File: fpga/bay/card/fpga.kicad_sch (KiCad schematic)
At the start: 0 parts

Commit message: card: fpga sheet — U14 XCAU15P placed and every ball resolved (rails, config, Quad 225, bank 84, unused banks/quads per 0011); passives next
Co-Authored-By: Claude Opus 5.5 (1M context) <noreply@anthropic.com>
Claude-Session: https://claude.ai/code/session_019QA2U79cSHCaAaMe6Km575
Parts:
- added U14: XCAU15P-2FFVB676E, symbol fw16-fpga-module:XCAU15P-FFVB676
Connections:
- new net +0V85_VCCINT: U14.K11 (VCCINT), U14.K13 (VCCINT), U14.K15 (VCCINT), U14.K17 (VCCINT), U14.L10 (VCCINT), U14.L12 (VCCINT), U14.L14 (VCCINT), U14.L16 (VCCINT), U14.L9 (VCCINT_IO), U14.M11 (VCCINT), U14.M13 (VCCINT), U14.M15 (VCCINT), U14.M17 (VCCINT), U14.M9 (VCCINT_IO), U14.N10 (VCCINT), U14.N12 (VCCINT), U14.N16 (VCCINT), U14.N9 (VCCINT_IO), U14.P11 (VCCINT), U14.P15 (VCCINT), U14.P17 (VCCINT), U14.P9 (VCCINT_IO), U14.R10 (VCCINT), U14.R12 (VCCINT), U14.R16 (VCCINT), U14.R9 (VCCBRAM), U14.T11 (VCCINT), U14.T15 (VCCINT), U14.T17 (VCCINT), U14.T9 (VCCBRAM), U14.U10 (VCCINT), U14.U12 (VCCINT), U14.U14 (VCCINT), U14.U16 (VCCINT), U14.U9 (VCCBRAM), U14.V11 (VCCINT), U14.V13 (VCCINT), U14.V15 (VCCINT), U14.V17 (VCCINT), U14.V9 (VCCBRAM)
- new net +0V9_MGTAVCC: U14.AA7 (MGTAVCC_R), U14.AC7 (MGTAVCC_R), U14.J7 (MGTAVCC_R), U14.L7 (MGTAVCC_R), U14.N7 (MGTAVCC_R), U14.W7 (MGTAVCC_R)
- new net +1V2_MGTAVTT: U14.A7 (MGTAVTT_R), U14.AB5 (MGTAVTT_R), U14.AD8 (MGTAVTTRCAL_R), U14.AE7 (MGTAVTT_R), U14.C7 (MGTAVTT_R), U14.E7 (MGTAVTT_R), U14.F5 (MGTAVTT_R), U14.G7 (MGTAVTT_R), U14.H5 (MGTAVTT_R), U14.K5 (MGTAVTT_R), U14.M5 (MGTAVTT_R), U14.P5 (MGTAVTT_R), U14.T5 (MGTAVTT_R), U14.V5 (MGTAVTT_R), U14.Y5 (MGTAVTT_R)
- new net +1V8: U14.AA11 (VCCO_0), U14.AA21 (VCCO_64), U14.AB18 (VCCO_64), U14.AD12 (VCCO_0), U14.AD22 (VCCO_64), U14.E14 (VCCO_86), U14.E24 (VCCO_66), U14.E9 (VCCO_85), U14.H10 (VCCO_85), U14.H15 (VCCO_86), U14.H25 (VCCO_66), U14.J22 (VCCO_66), U14.M18 (VCCAUX), U14.N18 (VCCAUX), U14.P18 (VCCAUX_IO), U14.P22 (VCCO_65), U14.R18 (VCCAUX_IO), U14.T18 (VCCAUX_IO), U14.U23 (VCCO_65), U14.Y24 (VCCO_65)
- new net +1V8_MGTVCCAUX: U14.R7 (MGTVCCAUX_R), U14.U7 (MGTVCCAUX_R)
- new net +3V3_IO: U14.AC15 (VCCO_84), U14.Y14 (VCCO_84)
- new net CLK100M: U14.AC13 (IO_L5P_HDGC_AD7P_84)
- new net FPGA_CCLK: U14.Y11 (CCLK_0)
- new net FPGA_CLKREQ_N: U14.AF15 (IO_L1N_AD11N_84)
- new net FPGA_D00: U14.AD11 (D00_MOSI_0)
- new net FPGA_D01: U14.AC12 (D01_DIN_0)
- new net FPGA_D02: U14.AC11 (D02_0)
- new net FPGA_D03: U14.AE11 (D03_0)
- new net FPGA_DONE: U14.AB11 (DONE_0)
- new net FPGA_FCS_B: U14.AA12 (RDWR_FCS_B_0)
- new net FPGA_INIT_B: U14.W10 (INIT_B_0)
- new net FPGA_M0: U14.AA10 (M0_0)
- new net FPGA_M1: U14.AA9 (M1_0)
- new net FPGA_M2: U14.AF12 (M2_0)
- new net FPGA_PROGRAM_B: U14.AB9 (PROGRAM_B_0)
- new net FPGA_PUDC_B: U14.W9 (PUDC_B_0)
- new net FPGA_TCK: U14.AE12 (TCK_0)
- new net FPGA_TDI: U14.AB12 (TDI_0)
- new net FPGA_TDO: U14.Y10 (TDO_0)
- new net FPGA_TH_ALERT: U14.AE13 (IO_L2P_AD10P_84)
- new net FPGA_TH_OVERT: U14.AF13 (IO_L2N_AD10N_84)
- new net FPGA_TMS: U14.AB10 (TMS_0)
- new net GND: U14.A1 (GND), U14.A11 (GND), U14.A16 (GND), U14.A2 (GND), U14.A21 (GND), U14.A26 (GND), U14.A5 (GND), U14.A6 (GND), U14.A8 (GND), U14.AA1 (GND), U14.AA16 (GND), U14.AA2 (GND), U14.AA26 (GND), U14.AA3 (GND), U14.AA6 (GND), U14.AA8 (GND), U14.AB1 (MGTHRXN3_224), U14.AB13 (GND), U14.AB2 (MGTHRXP3_224), U14.AB23 (GND), U14.AB3 (GND), U14.AB4 (GND), U14.AB8 (GND), U14.AC1 (GND), U14.AC10 (GND), U14.AC2 (GND), U14.AC20 (GND), U14.AC25 (GND), U14.AC3 (GND), U14.AC6 (GND), U14.AC8 (GND), U14.AC9 (GND), U14.AD1 (MGTHRXN2_224), U14.AD10 (GND), U14.AD17 (GND), U14.AD2 (MGTHRXP2_224), U14.AD3 (GND), U14.AD4 (GND), U14.AD5 (GND), U14.AE1 (GND), U14.AE10 (GND), U14.AE14 (GND), U14.AE19 (GND), U14.AE2 (GND), U14.AE24 (GND), U14.AE3 (MGTHRXN1_224), U14.AE4 (MGTHRXP1_224), U14.AE5 (GND), U14.AE6 (GND), U14.AF1 (MGTHRXN0_224), U14.AF10 (GND), U14.AF11 (GND), U14.AF16 (GND), U14.AF2 (MGTHRXP0_224), U14.AF21 (GND), U14.AF26 (GND), U14.AF3 (GND), U14.AF4 (GND), U14.AF5 (GND), U14.AF8 (GND), U14.AF9 (GND), U14.B13 (GND), U14.B18 (GND), U14.B23 (GND), U14.B3 (GND), U14.B4 (GND), U14.B5 (GND), U14.B8 (GND), U14.C1 (GND), U14.C10 (GND), U14.C15 (GND), U14.C2 (GND), U14.C25 (GND), U14.C5 (GND), U14.C6 (GND), U14.C8 (GND), U14.D12 (GND), U14.D22 (GND), U14.D3 (GND), U14.D4 (GND), U14.D5 (GND), U14.D8 (GND), U14.E1 (GND), U14.E19 (GND), U14.E2 (GND), U14.E3 (GND), U14.E6 (GND), U14.E8 (GND), U14.F1 (MGTHRXN3_226), U14.F11 (GND), U14.F16 (GND), U14.F2 (MGTHRXP3_226), U14.F21 (GND), U14.F26 (GND), U14.F3 (GND), U14.F4 (GND), U14.F8 (GND), U14.G1 (GND), U14.G13 (GND), U14.G2 (GND), U14.G23 (GND), U14.G3 (GND), U14.G6 (GND), U14.G8 (GND), U14.H1 (MGTHRXN2_226), U14.H2 (MGTHRXP2_226), U14.H20 (GND), U14.H3 (GND), U14.H4 (GND), U14.H8 (GND), U14.J1 (GND), U14.J17 (GND), U14.J2 (GND), U14.J3 (GND), U14.J6 (GND), U14.J8 (GND), U14.K1 (MGTHRXN1_226), U14.K12 (GND), U14.K14 (GND), U14.K16 (GND), U14.K19 (GND), U14.K2 (MGTHRXP1_226), U14.K24 (GND), U14.K3 (GND), U14.K4 (GND), U14.K8 (GND), U14.L1 (GND), U14.L11 (GND), U14.L13 (GND), U14.L15 (GND), U14.L17 (GND), U14.L2 (GND), U14.L21 (GND), U14.L26 (GND), U14.L3 (GND), U14.L6 (GND), U14.L8 (GND), U14.M1 (MGTHRXN0_226), U14.M10 (GND), U14.M12 (GND), U14.M14 (GND), U14.M16 (GND), U14.M2 (MGTHRXP0_226), U14.M23 (GND), U14.M3 (GND), U14.M4 (GND), U14.M8 (GND), U14.N1 (GND), U14.N11 (GND), U14.N15 (GND), U14.N17 (GND), U14.N2 (GND), U14.N20 (GND), U14.N25 (GND), U14.N3 (GND), U14.N6 (GND), U14.N8 (GND), U14.P10 (GND), U14.P12 (GND), U14.P16 (GND), U14.P3 (GND), U14.P4 (GND), U14.P8 (GND), U14.R1 (GND), U14.R11 (GND), U14.R15 (GND), U14.R17 (GND), U14.R19 (GND), U14.R2 (GND), U14.R24 (GND), U14.R3 (GND), U14.R6 (GND), U14.R8 (GND), U14.T10 (GND), U14.T12 (GND), U14.T13 (DXN), U14.T14 (DXP), U14.T16 (GND), U14.T21 (GND), U14.T26 (GND), U14.T3 (GND), U14.T4 (GND), U14.T8 (GND), U14.U1 (GND), U14.U11 (GND), U14.U13 (GND), U14.U15 (GND), U14.U17 (GND), U14.U18 (GND), U14.U2 (GND), U14.U3 (GND), U14.U6 (GND), U14.U8 (GND), U14.V10 (GND), U14.V12 (GND), U14.V14 (GND), U14.V16 (GND), U14.V20 (GND), U14.V25 (GND), U14.V3 (GND), U14.V4 (GND), U14.V8 (GND), U14.W1 (GND), U14.W11 (RSVDGND), U14.W17 (GND), U14.W2 (GND), U14.W22 (GND), U14.W3 (GND), U14.W6 (GND), U14.W8 (GND), U14.Y12 (POR_OVERRIDE), U14.Y19 (GND), U14.Y3 (GND), U14.Y4 (GND), U14.Y8 (GND), U14.Y9 (VBATT)
- new net GNDADC: U14.N13 (GNDADC), U14.P13 (VREFN), U14.P14 (VP), U14.R13 (VN), U14.R14 (VREFP)
- new net GT_REFCLK0_N: U14.V6 (MGTREFCLK0N_225)
- new net GT_REFCLK0_P: U14.V7 (MGTREFCLK0P_225)
- new net GT_REFCLK1_N: U14.T6 (MGTREFCLK1N_225)
- new net GT_REFCLK1_P: U14.T7 (MGTREFCLK1P_225)
- new net GT_TX0_N: U14.AA4 (MGTHTXN0_225)
- new net GT_TX0_P: U14.AA5 (MGTHTXP0_225)
- new net GT_TX1_N: U14.W4 (MGTHTXN1_225)
- new net GT_TX1_P: U14.W5 (MGTHTXP1_225)
- new net GT_TX2_N: U14.U4 (MGTHTXN2_225)
- new net GT_TX2_P: U14.U5 (MGTHTXP2_225)
- new net GT_TX3_N: U14.R4 (MGTHTXN3_225)
- new net GT_TX3_P: U14.R5 (MGTHTXP3_225)
- new net LED_HB: U14.W12 (IO_L12P_AD0P_84)
- new net LED_LINK: U14.W13 (IO_L12N_AD0N_84)
- new net MGT_RREF: U14.AD9 (MGTRREF_R)
- new net PEX_RST#: U14.AF14 (IO_L1P_AD11P_84)
- new net PEX_TX0_N: U14.Y1 (MGTHRXN0_225)
- new net PEX_TX0_P: U14.Y2 (MGTHRXP0_225)
- new net PEX_TX1_N: U14.V1 (MGTHRXN1_225)
- new net PEX_TX1_P: U14.V2 (MGTHRXP1_225)
- new net PEX_TX2_N: U14.T1 (MGTHRXN2_225)
- new net PEX_TX2_P: U14.T2 (MGTHRXP2_225)
- new net PEX_TX3_N: U14.P1 (MGTHRXN3_225)
- new net PEX_TX3_P: U14.P2 (MGTHRXP3_225)
- new net PPS_IN: U14.AB15 (IO_L6P_HDGC_AD6P_84)
- new net SENSE_ALERT#: U14.AD14 (IO_L4N_AD8N_84)
- new net SENSE_SCL: U14.AD15 (IO_L3P_AD9P_84)
- new net SENSE_SDA: U14.AE15 (IO_L3N_AD9N_84)
- new net VCCADC: U14.N14 (VCCADC)
- no-connect marks 0 -> 244

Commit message: card: fpga sheet complete — decoupling, SYSMON filter, RCAL, PCIe AC caps, SiT8008/SiT9121 clocks, U.FL PPS/ref input, LEDs; card ERC 0 errors
Co-Authored-By: Claude Opus 5.5 (1M context) <noreply@anthropic.com>
Claude-Session: https://claude.ai/code/session_019QA2U79cSHCaAaMe6Km575
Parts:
- added C46: 330u/2.5V polymer, Capacitor_Tantalum_SMD:CP_EIA-7343-31_Kemet-D, symbol Device:C_Polarized
- added C47: 100u/4V, Capacitor_SMD:C_1210_3225Metric, symbol Device:C
- added C48, C49, C60, C63, C64: 47u/4V, Capacitor_SMD:C_1206_3216Metric, symbol Device:C
- added C50, C51, C61, C62, C65, C66, C67, C68, C69: 10u/4V, Capacitor_SMD:C_0603_1608Metric, symbol Device:C
- added C52, C53, C54, C55, C56, C57, C58, C59, C76, C87: 100n, Capacitor_SMD:C_0402_1005Metric, symbol Device:C
- added C70: 47u/6.3V, Capacitor_SMD:C_1206_3216Metric, symbol Device:C
- added C71: 10u/6.3V, Capacitor_SMD:C_0603_1608Metric, symbol Device:C
- added C72, C73, C74: 4.7u/6.3V, Capacitor_SMD:C_0603_1608Metric, symbol Device:C
- added C75: 470n, Capacitor_SMD:C_0402_1005Metric, symbol Device:C
- added C77, C78, C79, C80, C81, C82, C83, C84: 220n, Capacitor_SMD:C_0402_1005Metric, symbol Device:C
- added C85, C86: 10n, Capacitor_SMD:C_0402_1005Metric, symbol Device:C
- added C88: 100n DNP, Capacitor_SMD:C_0402_1005Metric, symbol Device:C
- added C89, C90: 10n DNP, Capacitor_SMD:C_0402_1005Metric, symbol Device:C
- added D1, D2: green, LED_SMD:LED_0603_1608Metric, symbol Device:LED
- added FB1, FB2: BLM18PG221SN1, Inductor_SMD:L_0603_1608Metric, symbol Device:FerriteBead
- added J5: U.FL PPS/10MHz/trigger, Connector_Coaxial:U.FL_Hirose_U.FL-R-SMT-1_Vertical, symbol Connector:Conn_Coaxial
- added R48: 100 1%, Resistor_SMD:R_0402_1005Metric, symbol Device:R
- added R49: 33, Resistor_SMD:R_0402_1005Metric, symbol Device:R
- added R50, R51: 1k, Resistor_SMD:R_0402_1005Metric, symbol Device:R
- added U15: TPD1E04U04DPY, Package_SON:Texas_DPY0002A_0.6x1mm_P0.65mm, symbol Power_Protection:TPD1E05U06DPY
- added Y1: SiT8008 100MHz 3.3V, Oscillator:Oscillator_SMD_SiT_PQFN-4Pin_2.0x1.6mm, symbol Oscillator:SiT8008xx-1x-xxE
- added Y2: SiT9121 100MHz LVDS DNP, Oscillator:Oscillator_SMD_SiTime_SiT9121-6Pin_3.2x2.5mm, symbol fw16-fpga-module:SiT9121
- U14: footprint (none) -> Package_BGA:BGA-676_27.0x27.0mm_Layout26x26_P1.0mm_Ball0.6mm_Pad0.5mm_NSMD
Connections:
- net +0V85_VCCINT: now also C46.1, C47.1, C48.1, C49.1, C50.1, C51.1, C52.1, C53.1, C54.1, C55.1, C56.1, C57.1, C58.1, C59.1
- net +0V9_MGTAVCC: now also C72.1
- net +1V2_MGTAVTT: now also C73.1, R48.1
- net +1V8: now also C60.1, C61.1, C62.1, C63.1, C64.1, C65.1, C66.1, C67.1, C68.1, C69.1, FB1.1
- net +1V8_MGTVCCAUX: now also C74.1
- net +3V3_IO: now also C70.1, C71.1, C87.1, C88.1, Y1.1 (OE), Y1.4 (Vdd), Y2.1 (OE), Y2.6 (VDD)
- net CLK100M: now also Y1.3 (OUT)
- net GND: now also C46.2, C47.2, C48.2, C49.2, C50.2, C51.2, C52.2, C53.2, C54.2, C55.2, C56.2, C57.2, C58.2, C59.2, C60.2, C61.2, C62.2, C63.2, C64.2, C65.2, C66.2, C67.2, C68.2, C69.2, C70.2, C71.2, C72.2, C73.2, C74.2, C87.2, C88.2, D1.1 (K), D2.1 (K), FB2.2, J5.2 (Ext), U15.2 (GND), Y1.2 (GND), Y2.3 (GND)
- net GNDADC: now also C75.2, C76.2, FB2.1
- net GT_REFCLK0_N: now also C86.2
- net GT_REFCLK0_P: now also C85.2
- net GT_REFCLK1_N: now also C90.2
- net GT_REFCLK1_P: now also C89.2
- net GT_TX0_N: now also C78.1
- net GT_TX0_P: now also C77.1
- net GT_TX1_N: now also C80.1
- net GT_TX1_P: now also C79.1
- net GT_TX2_N: now also C82.1
- net GT_TX2_P: now also C81.1
- net GT_TX3_N: now also C84.1
- net GT_TX3_P: now also C83.1
- net LED_HB: now also R50.1
- net LED_LINK: now also R51.1
- net MGT_RREF: now also R48.2
- net PPS_IN: now also R49.2
- net VCCADC: now also C75.1, C76.1, FB1.2
- new net BENCH_CLK_N: C90.1, Y2.5 (~{OUT})
- new net BENCH_CLK_P: C89.1, Y2.4 (OUT)
- new net LED_HB_A: D1.2 (A), R50.2
- new net LED_LINK_A: D2.2 (A), R51.2
- new net PEX_REFCLK_N: C86.1
- new net PEX_REFCLK_P: C85.1
- new net PEX_RX0_N: C78.2
- new net PEX_RX0_P: C77.2
- new net PEX_RX1_N: C80.2
- new net PEX_RX1_P: C79.2
- new net PEX_RX2_N: C82.2
- new net PEX_RX2_P: C81.2
- new net PEX_RX3_N: C84.2
- new net PEX_RX3_P: C83.2
- new net PPS_RAW: J5.1 (In), R49.1, U15.1 (I/O)

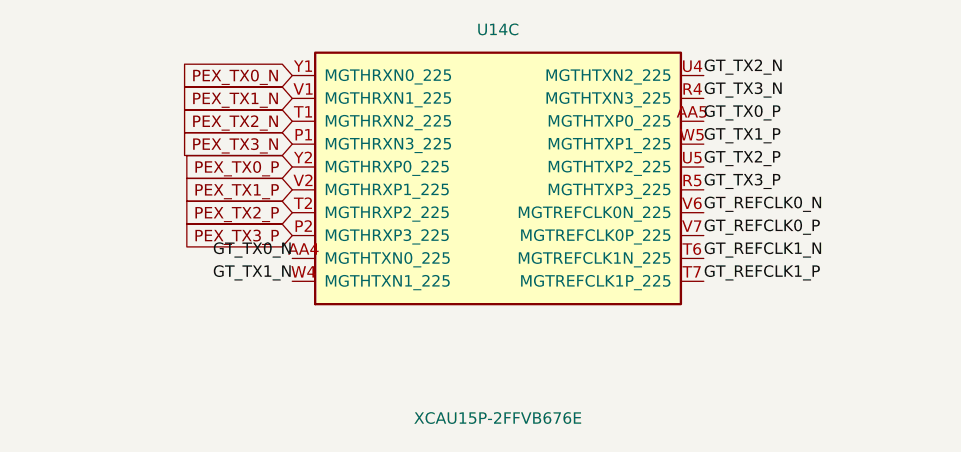
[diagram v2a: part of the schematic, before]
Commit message: card: swap PCIe lanes to match XDMA (lane n = Quad 225 ch 3-n); pinplan + pin XDC + fpga sheet; placed-pin checks in power.tcl/pinplan_check; 0010 amended
Co-Authored-By: Claude Opus 5.5 (1M context) <noreply@anthropic.com>
Claude-Session: https://claude.ai/code/session_019QA2U79cSHCaAaMe6Km575
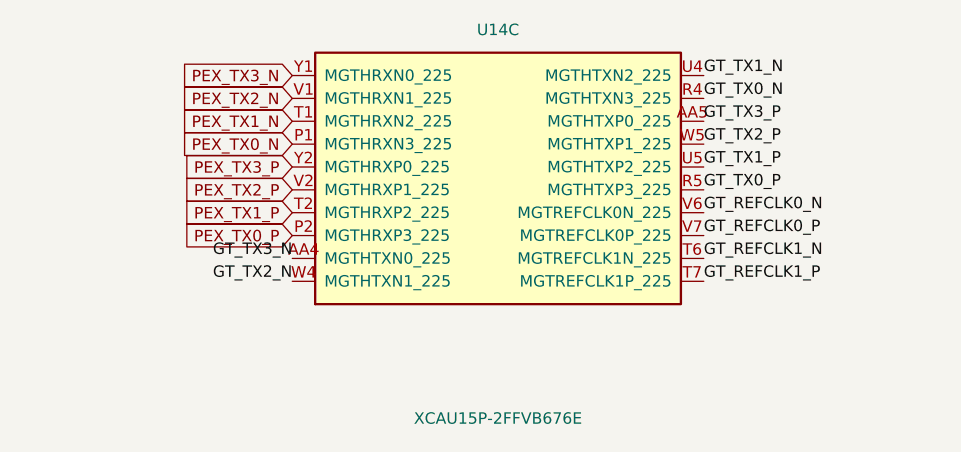
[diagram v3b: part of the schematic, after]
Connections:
- net GT_TX0_N: now also U14.R4 (MGTHTXN3_225); no longer U14.AA4 (MGTHTXN0_225)
- net GT_TX0_P: now also U14.R5 (MGTHTXP3_225); no longer U14.AA5 (MGTHTXP0_225)
- net GT_TX1_N: now also U14.U4 (MGTHTXN2_225); no longer U14.W4 (MGTHTXN1_225)
- net GT_TX1_P: now also U14.U5 (MGTHTXP2_225); no longer U14.W5 (MGTHTXP1_225)
- net GT_TX2_N: now also U14.W4 (MGTHTXN1_225); no longer U14.U4 (MGTHTXN2_225)
- net GT_TX2_P: now also U14.W5 (MGTHTXP1_225); no longer U14.U5 (MGTHTXP2_225)
- net GT_TX3_N: now also U14.AA4 (MGTHTXN0_225); no longer U14.R4 (MGTHTXN3_225)
- net GT_TX3_P: now also U14.AA5 (MGTHTXP0_225); no longer U14.R5 (MGTHTXP3_225)
- net PEX_TX0_N: now also U14.P1 (MGTHRXN3_225); no longer U14.Y1 (MGTHRXN0_225)
- net PEX_TX0_P: now also U14.P2 (MGTHRXP3_225); no longer U14.Y2 (MGTHRXP0_225)
- net PEX_TX1_N: now also U14.T1 (MGTHRXN2_225); no longer U14.V1 (MGTHRXN1_225)
- net PEX_TX1_P: now also U14.T2 (MGTHRXP2_225); no longer U14.V2 (MGTHRXP1_225)
- net PEX_TX2_N: now also U14.V1 (MGTHRXN1_225); no longer U14.T1 (MGTHRXN2_225)
- net PEX_TX2_P: now also U14.V2 (MGTHRXP1_225); no longer U14.T2 (MGTHRXP2_225)
- net PEX_TX3_N: now also U14.Y1 (MGTHRXN0_225); no longer U14.P1 (MGTHRXN3_225)
- net PEX_TX3_P: now also U14.Y2 (MGTHRXP0_225); no longer U14.P2 (MGTHRXP3_225)

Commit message: card: heatsink nuts H1-H4 (Wurth 9774030243R, footprint from datasheet land pattern) on the fpga sheet; 0012 part choice
Co-Authored-By: Claude Opus 5.5 (1M context) <noreply@anthropic.com>
Claude-Session: https://claude.ai/code/session_019QA2U79cSHCaAaMe6Km575
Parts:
- added H1, H2, H3, H4: M2 SMT nut 9774030243R, fw16-fpga-module:Wurth_WA-SMSI_M2_9774030243R, symbol Mechanical:MountingHole_Pad
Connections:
- net GND: now also H1.1, H2.1, H3.1, H4.1
